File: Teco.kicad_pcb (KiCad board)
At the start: 2 copper layers, 42 x 24 mm, 55 parts, among them Q2 BC848, Q3 IRLML9303, SW1 BUTTON

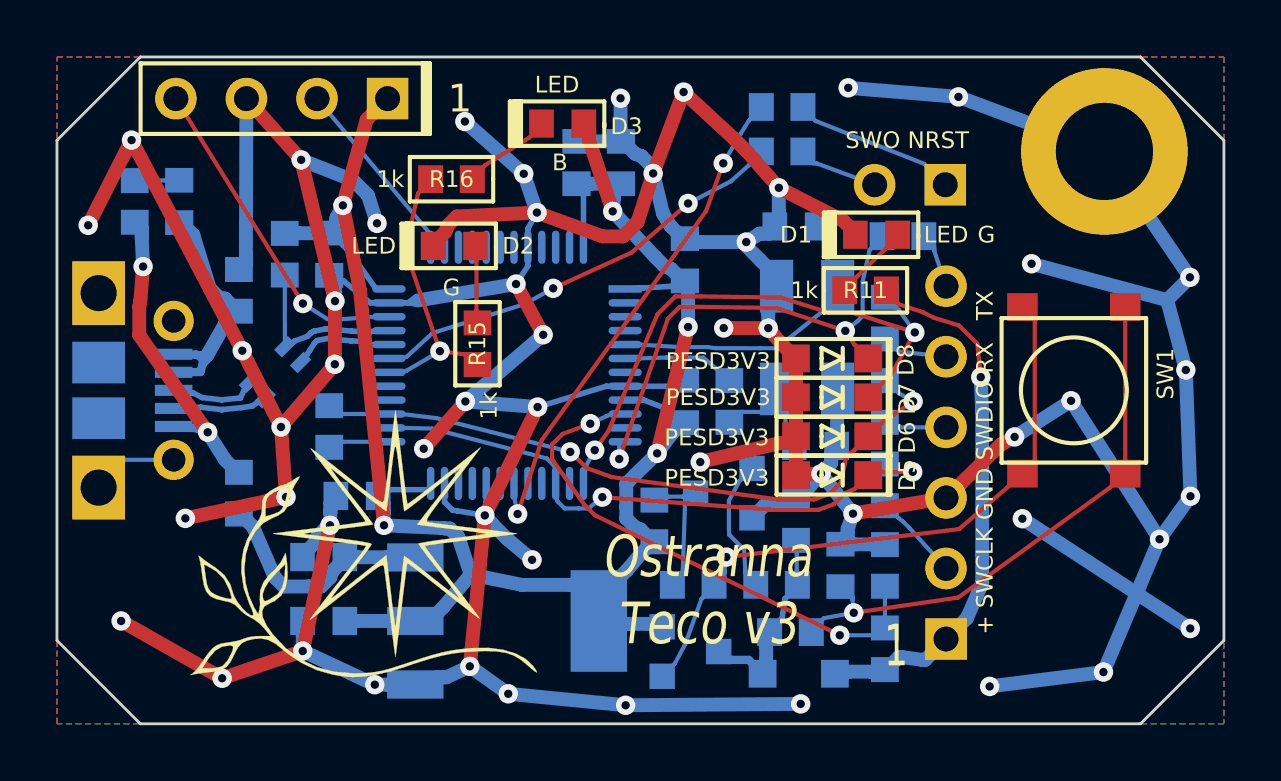
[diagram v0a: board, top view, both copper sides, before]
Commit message: v3.1: + Pull-up on RX + legend
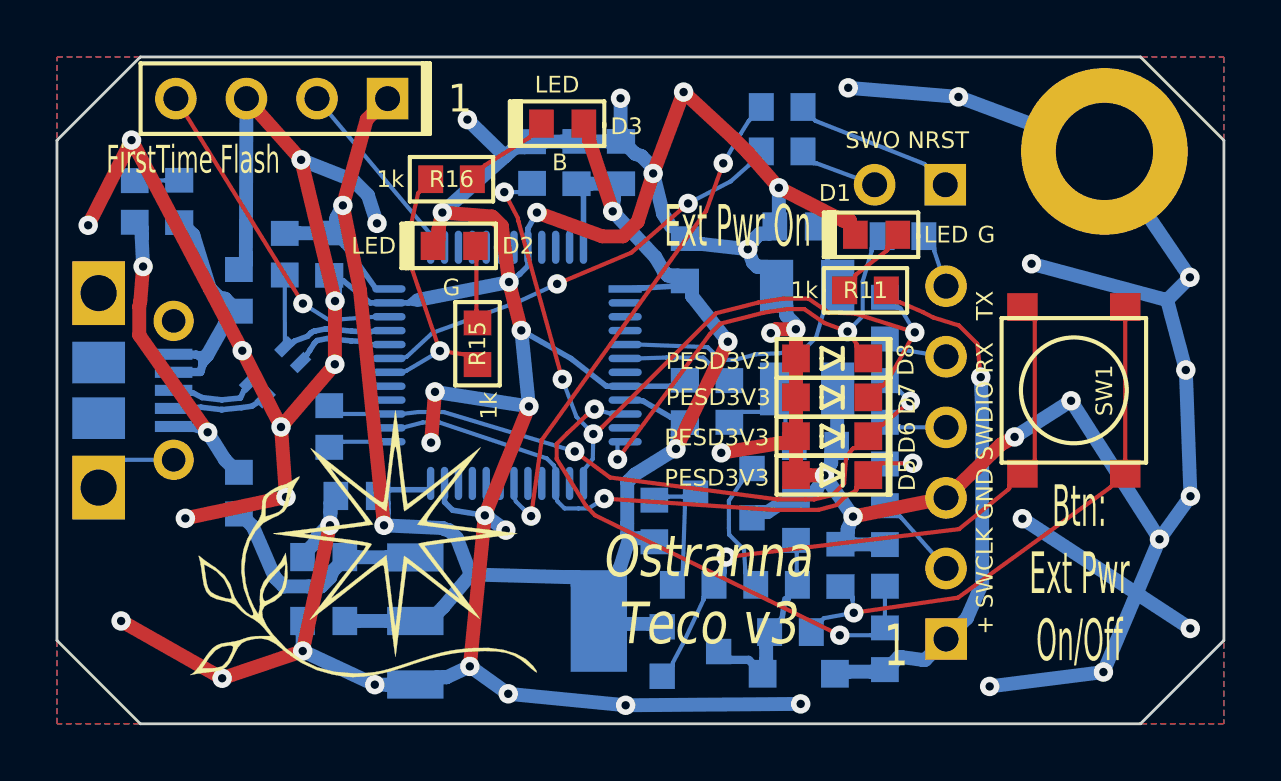
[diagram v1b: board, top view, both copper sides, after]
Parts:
- added R7: 100k, Resistors:RES_0603, B.Cu at (130.1, 74.8)
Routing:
- net /RXD: track 21.0 -> 30.7 mm, vias 2 -> 4
- net +3v3: track 74.4 -> 78.6 mm
- net GND: track 250.8 -> 252.6 mm
- net /TXD: track 18.1 -> 17.0 mm
- net /GNDIN: track 9.67 -> 10.5 mm
- net Net-(C11-Pad1): track 11.0 -> 11.7 mm
- net /T_JTCK: track 22.1 -> 22.7 mm
- net /T_JTMS: track 24.6 -> 25.1 mm
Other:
- board text added: "Btn: Ext Pwr On/Off"
- board text added: "Ext Pwr On"
- board text added: "FirstTime Flash"
